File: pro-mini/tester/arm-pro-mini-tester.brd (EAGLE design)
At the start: 49.5 x 33 mm, 38 parts, among them U1 ARM-PRO-MINI

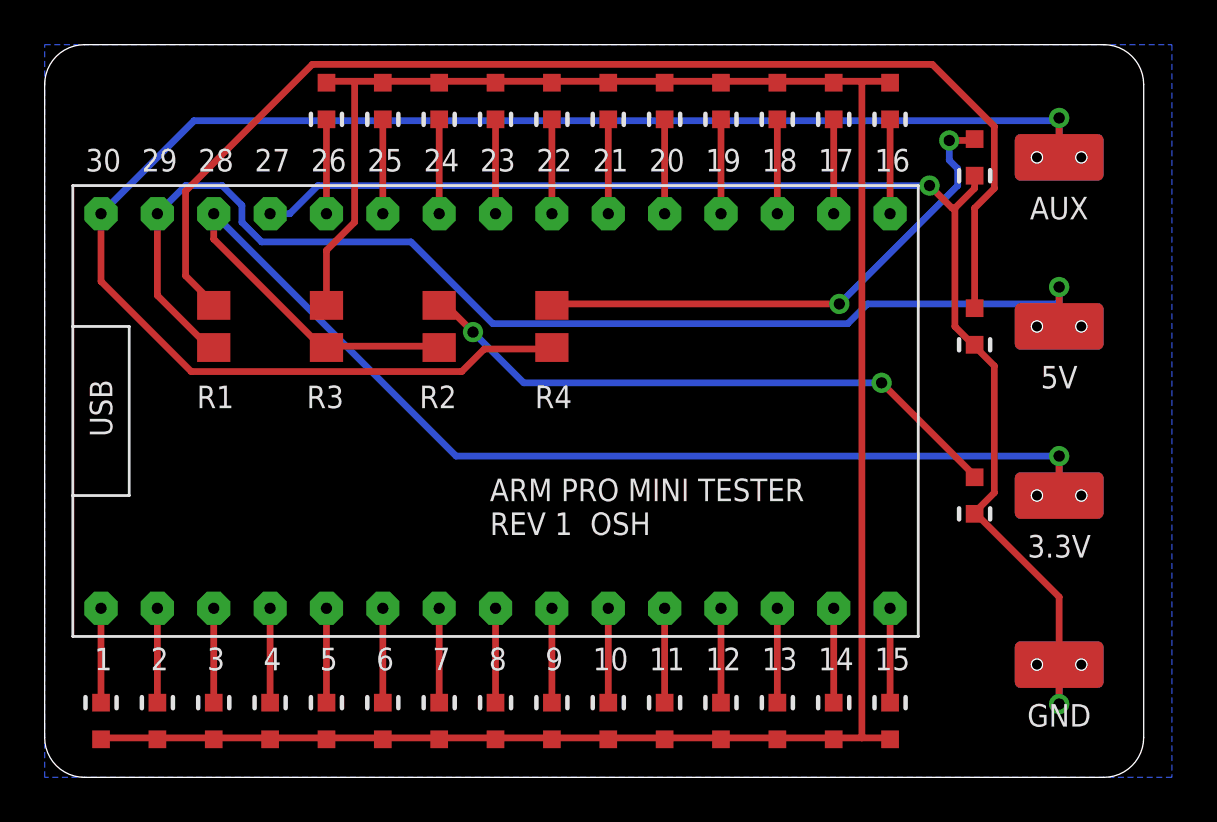
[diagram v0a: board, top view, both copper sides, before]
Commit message: Increased pogo pin holes, added RST and ISP buttons.
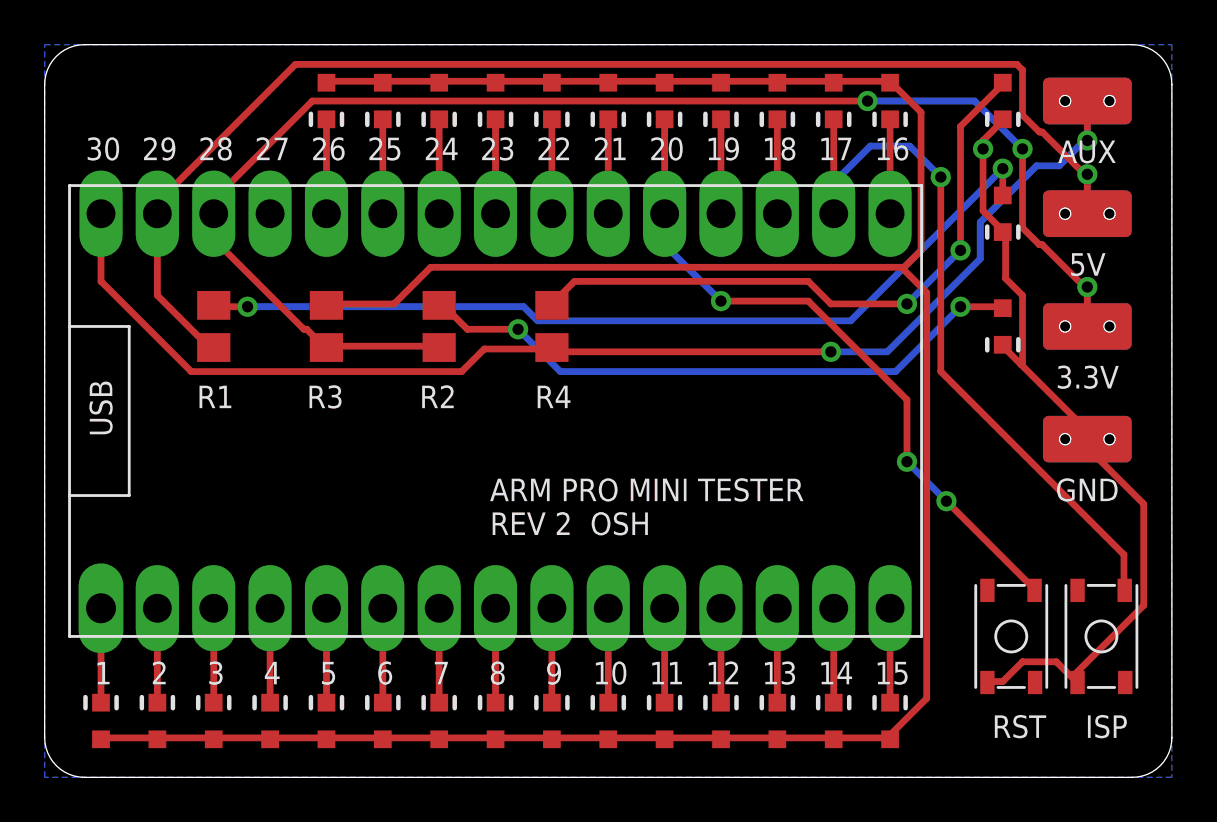
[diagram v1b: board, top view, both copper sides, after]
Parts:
- added S1, S2: PUSH_BUTTON, arm-pro-mini:PUSH_BUTTON
- moved TP1 10.2 mm to (47.0, 15.2)
- moved D19 7.73 mm to (43.2, 20.3)
- moved TP2 7.73 mm to (47.0, 20.3)
- moved D16 5.24 mm to (43.2, 25.4)
- moved TP3 5.24 mm to (47.0, 25.4)
- moved D17 2.84 mm to (43.2, 30.5)
- moved TP4 2.84 mm to (47.0, 30.5)
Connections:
- removed net N$18: D29.C, U1.17
- removed net N$21: D25.C, U1.20
- new net ISP: D29.C, S2.B2, U1.17
- new net RST: D25.C, S1.B2, U1.20
- net GND: now also S1.A1, S2.A1
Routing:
- net ISP: track 0.00 -> 33.8 mm, vias 0 -> 1
- net RST: track 0.00 -> 30.4 mm, vias 0 -> 3
- net GND: track 60.5 -> 36.3 mm, vias 2 -> 1
- net N$27: track 103.2 -> 121.3 mm
- net EXT: track 74.1 -> 58.3 mm, vias 1 -> 2
- net N$31: track 54.2 -> 39.9 mm, vias 0 -> 2
- net +3.3V: track 59.7 -> 64.4 mm, vias 1 -> 3
- net N$28: track 24.0 -> 28.7 mm
- net N$21: track 4.26 -> 0.00 mm
- net N$18: track 4.26 -> 0.00 mm
- net +5V: track 56.2 -> 59.0 mm
- net N$29: track 27.4 -> 27.9 mm
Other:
- board size 49.5 x 33 mm -> 50.8 x 33 mm
- board text added: "ARM PRO MINI TESTER REV 2 OSH"
- board text added: "ISP"
- board text added: "RST"
- board text removed: "ARM PRO MINI TESTER REV 1 OSH"

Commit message: Reduced pogo hole sizes from 1.35 mm to ~1mm (40 mil).
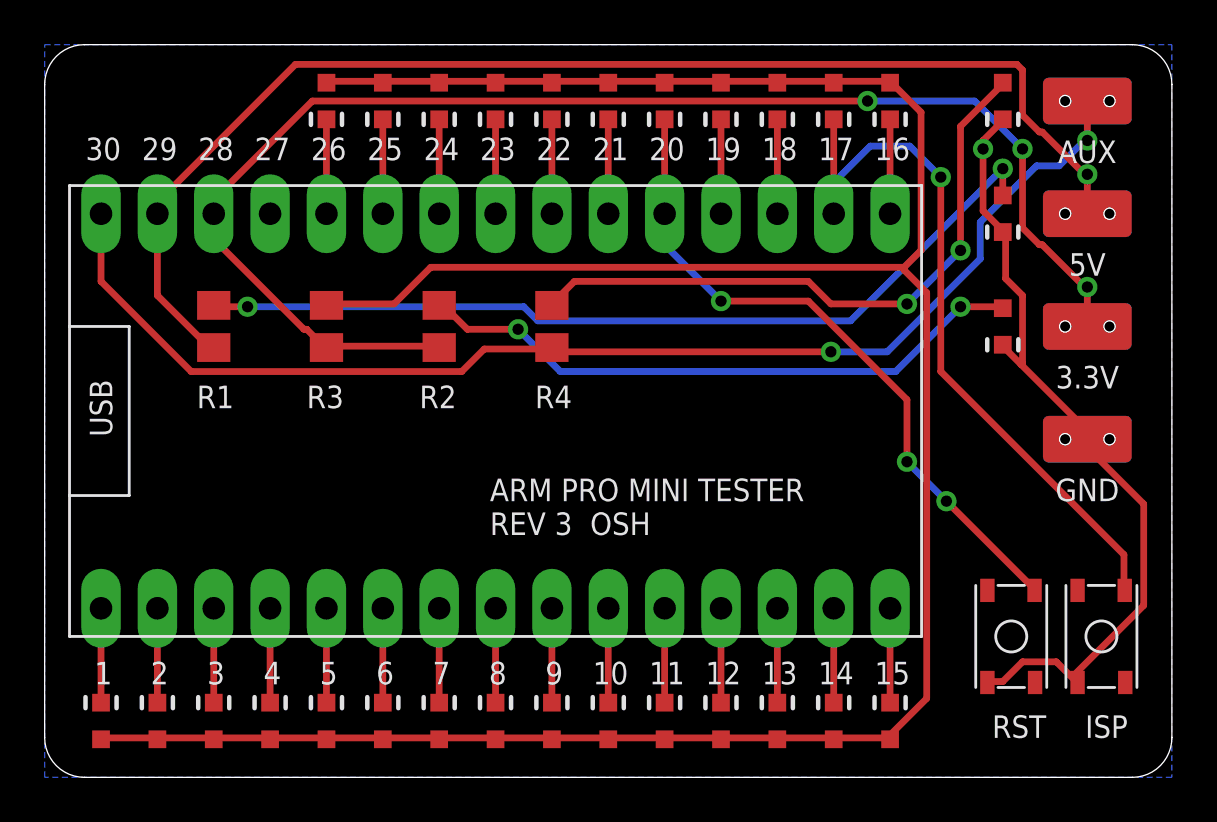
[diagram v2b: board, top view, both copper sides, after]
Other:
- board text added: "ARM PRO MINI TESTER REV 3 OSH"
- board text removed: "ARM PRO MINI TESTER REV 2 OSH"
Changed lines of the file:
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@@
 <wire x1="49.022" y1="33.02" x2="50.8" y2="31.22395" width="0.0254" layer="20" curve="-90"/>
 <text x="20.066" y="10.922" size="1.016" layer="21" font="vector" ratio="10">ARM PRO MINI TESTER
-REV 2  OSH</text>
+REV 3  OSH</text>
 <text x="2.6416" y="4.191" size="1.016" layer="21" font="vector" ratio="10" align="bottom-center">1</text>
 <text x="5.1816" y="4.191" size="1.016" layer="21" font="vector" ratio="10" align="bottom-center">2</text>

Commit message: Fixed the tester board. Updated self test for a slow LED scanning.
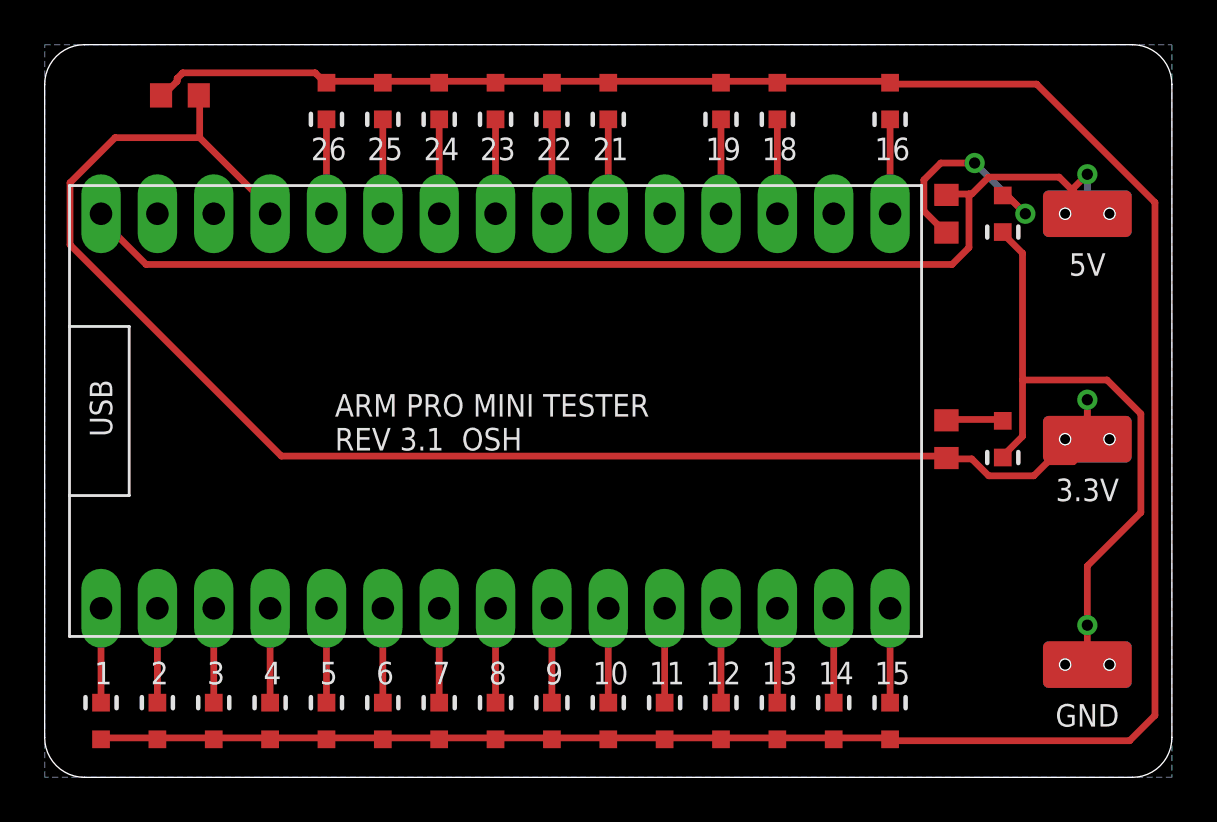
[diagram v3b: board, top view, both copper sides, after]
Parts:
- removed D27, D28, D29, D30: (no value), arm-pro-mini-tester:LED0603
- removed R4: (no value), arm-pro-mini-tester:R0805
- removed S1, S2: PUSH_BUTTON, arm-pro-mini:PUSH_BUTTON
- removed TP4: TEST-POINT, arm-pro-mini-tester:TEST-POINT
- added D18: (no value), arm-pro-mini-tester:LED0603
- R1, R2, R3: value (none) -> 1k5; device arm-pro-mini-tester:R0805 -> resistor:R0603
- moved D16 30.9 mm to (12.7, 30.5)
- moved R3 28.4 mm to (40.6, 25.4)
- moved D17 27.9 mm to (15.2, 30.5)
- moved D19 25.0 mm to (20.3, 30.5)
- moved R2 23.4 mm to (40.6, 15.2)
- moved D25 21.6 mm to (43.2, 15.2)
- moved D26 18.5 mm to (43.2, 25.4)
- moved D24 15.2 mm to (38.1, 30.5)
- moved D2 15.2 mm to (5.08, 2.54)
- moved D3 15.2 mm to (7.62, 2.54)
- moved D23 12.7 mm to (33.0, 30.5)
- moved D22 12.7 mm to (30.5, 30.5)
- moved R1 10.5 mm to (6.10, 30.7), turned to 0 degrees
- moved D20 10.2 mm to (22.9, 30.5)
- moved TP1 10.2 mm to (47.0, 5.08)
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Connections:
- removed net EXT: R4.1, TP4.A, TP4.B, U1.30
- removed net ISP: D29.C, S2.B2, U1.17
- removed net N$28: D17.A, R4.2
- removed net RST: D25.C, S1.B2, U1.20
- net +3.3V: now also R1.2, U1.27; no longer R3.2, U1.28
- net +5V: now also R3.1, U1.30; no longer R1.1, U1.29
- net GND: now also D25.C, D26.C, U1.28; no longer D16.C, D17.C, D19.C, S1.A1, S2.A1, U1.27
- net N$10: now also D11.C; no longer D10.C
- net N$11: now also D10.C; no longer D11.C
- net N$12: now also D6.C; no longer D8.C
- net N$13: now also D7.C; no longer D9.C
- net N$14: now also D9.C; no longer D3.C
- net N$15: now also D8.C; no longer D2.C
- net N$16: now also D19.C; no longer D23.C
- net N$17: now also D24.C; no longer D30.C
- net N$19: now also D23.C; no longer D28.C
- net N$2: now also D2.C; no longer D5.C
- net N$20: now also D22.C; no longer D27.C
- net N$22: now also D21.C; no longer D26.C
- net N$23: now also D20.C; no longer D24.C
- net N$24: now also D18.C; no longer D22.C
- net N$25: now also D17.C; no longer D21.C
- net N$26: now also D16.C; no longer D20.C
- net N$27: now also D16.A, D17.A, D18.A, D19.A, R1.1; no longer D25.A, D26.A, D27.A, D28.A, D29.A, D30.A, R3.1
- net N$29: now also D25.A; no longer D19.A
- net N$3: now also D3.C; no longer D4.C
- net N$31: now also D26.A, R3.2; no longer D16.A, R1.2
- net N$4: now also D4.C; no longer D6.C
- net N$5: now also D5.C; no longer D7.C
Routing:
- net EXT: track 58.3 -> 0.00 mm, vias 2 -> 0
- net ISP: track 33.8 -> 0.00 mm, vias 1 -> 0
- net RST: track 30.4 -> 0.00 mm, vias 3 -> 0
- net N$31: track 39.9 -> 10.1 mm
- net N$28: track 28.7 -> 0.00 mm, vias 2 -> 0
- net N$29: track 27.9 -> 2.64 mm, vias 2 -> 0
- net GND: track 36.3 -> 29.2 mm
- net +3.3V: track 64.4 -> 70.8 mm, vias 3 -> 1
- net +5V: track 59.0 -> 53.3 mm
- net N$27: track 121.3 -> 120.6 mm
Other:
- board text added: "ARM PRO MINI TESTER REV 3.1 OSH"
- board text removed: "17"
- board text removed: "20"
- board text removed: "27"
- board text removed: "28"
- board text removed: "29"
- board text removed: "30"
- board text removed: "ARM PRO MINI TESTER REV 3 OSH"
- board text removed: "AUX"
- board text removed: "ISP"
- board text removed: "RST"
